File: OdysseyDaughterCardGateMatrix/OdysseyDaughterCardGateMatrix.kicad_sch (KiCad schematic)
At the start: 18 parts

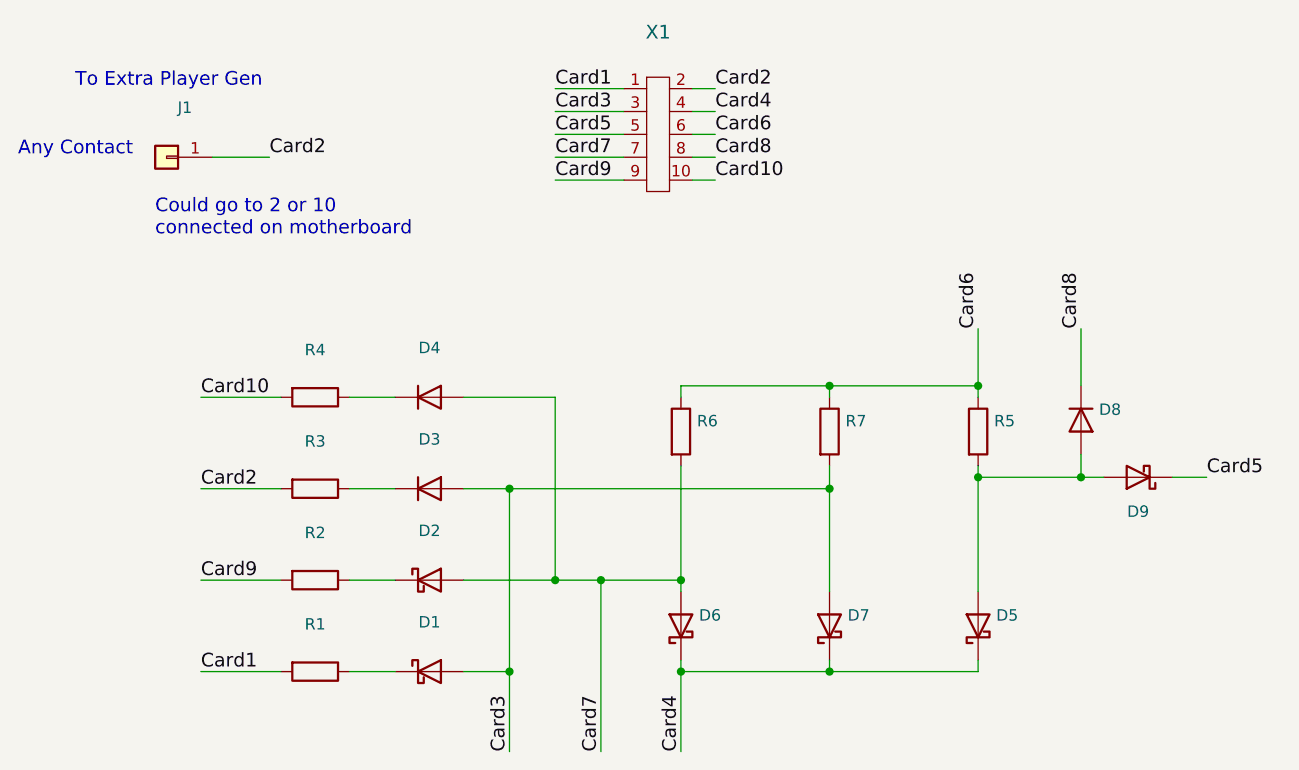
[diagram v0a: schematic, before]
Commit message: OdysseyDaughterCardGateMatrix wider transistor footprint, add logo, generate pdf, images, 3d models
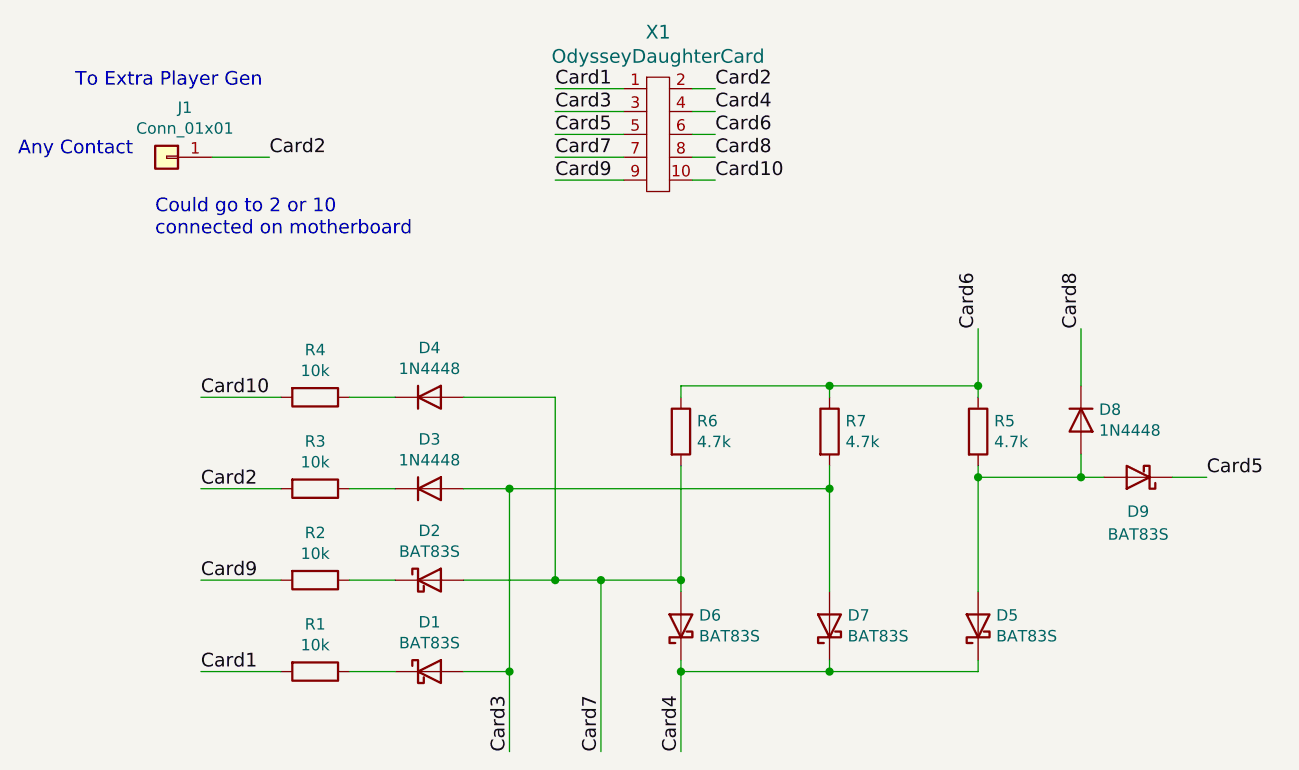
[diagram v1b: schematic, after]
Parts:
- D1, D2, D5, D6, D7, D9: value (none) -> BAT83S; footprint (none) -> Diode_THT:D_DO-41_SOD81_P7.62mm_Horizontal
- D3, D4, D8: value (none) -> 1N4448; footprint (none) -> Diode_THT:D_DO-35_SOD27_P7.62mm_Horizontal
- J1: value (none) -> Conn_01x01; footprint (none) -> Connector_PinHeader_2.54mm:PinHeader_1x01_P2.54mm_Vertical
- R1, R2, R3, R4: value (none) -> 10k; footprint (none) -> Resistor_THT:R_Axial_DIN0207_L6.3mm_D2.5mm_P7.62mm_Horizontal
- R5, R6, R7: value (none) -> 4.7k; footprint (none) -> Resistor_THT:R_Axial_DIN0207_L6.3mm_D2.5mm_P7.62mm_Horizontal
- X1: value (none) -> OdysseyDaughterCard; footprint (none) -> Odyssey_Daughter_Card:Odyssey_Daughter_Card
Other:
- company: University of Pittsburgh - Odyssey Restoration Project -> University of Pittsburgh - OdysseyNow
